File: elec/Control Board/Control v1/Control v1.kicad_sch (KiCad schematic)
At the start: 24 parts, among them J10 Conn_02x12_Odd_Even, J12 Screw_Terminal_01x02, J13 Screw_Terminal_01x02, J14 Screw_Terminal_01x02, J2 DB9_Female_MountingHoles, J3 Conn_01x08, J4 Conn_01x08, J5 Conn_01x08, J6 Conn_01x08, J7 Conn_01x08, J8 Conn_02x18_Odd_Even, J9 Conn_01x10_MountingPin

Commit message: Add footrpint to Max31850 module.
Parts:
- renumbered J2 to J1, J12 to J10, J13 to J11, J14 to J12, J3 to J2, J4 to J3, J5 to J4, J6 to J5, J7 to J6, J8 to J7, J9 to J8, J10 to J9
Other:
- note removed: "A change."
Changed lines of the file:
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@@
     (effects (font (size 0.635 0.635)) (justify left bottom))
-  )
-  (text "A change." (at 365.76 125.73 0)
-    (effects (font (size 1.27 1.27)) (justify left bottom))
   )
   (text "To chassis mounted +24V." (at 403.86 224.79 0)
@@
     )
   )
-  (global_label "aGlobal" (shape input) (at 325.12 69.85 0) (fields_autoplaced)
-    (effects (font (size 1.27 1.27)) (justify left))
-    (property "Intersheetrefs" "${INTERSHEET_REFS}" (at 335.2222 69.85 0)
-      (effects (font (size 1.27 1.27)) (justify left) hide)
-    )
-  )
   (global_label "BLOWER_TACH" (shape input) (at 316.23 199.39 180) (fields_autoplaced)
     (effects (font (size 1.27 1.27)) (justify right))
@@
   (symbol (lib_id "Connector_Generic:Conn_02x18_Odd_Even") (at 275.59 138.43 0) (unit 1)
     (in_bom yes) (on_board yes) (dnp no) (fields_autoplaced)
-    (property "Reference" "J8" (at 276.86 111.76 0)
+    (property "Reference" "J7" (at 276.86 111.76 0)
       (effects (font (size 1.27 1.27)))
     )
@@
       (project "Control v1"
         (path "/c68c9deb-8d4d-42f0-adf8-4d3022f4ee59"
-          (reference "J8") (unit 1)
+          (reference "J7") (unit 1)
         )
       )
@@
   (symbol (lib_id "Connector:Screw_Terminal_01x02") (at 394.97 226.06 0) (unit 1)
     (in_bom yes) (on_board yes) (dnp no) (fields_autoplaced)
-    (property "Reference" "J13" (at 397.51 226.695 0)
+    (property "Reference" "J11" (at 397.51 226.695 0)
       (effects (font (size 1.27 1.27)) (justify left))
     )
@@
       (project "Control v1"
         (path "/c68c9deb-8d4d-42f0-adf8-4d3022f4ee59"
-          (reference "J13") (unit 1)
+          (reference "J11") (unit 1)
         )
       )
@@
   (symbol (lib_id "power:+12V") (at 382.27 190.5 0) (unit 1)
     (in_bom yes) (on_board yes) (dnp no) (fields_autoplaced)
-    (property "Reference" "#PWR017" (at 382.27 194.31 0)
+    (property "Reference" "#PWR016" (at 382.27 194.31 0)
       (effects (font (size 1.27 1.27)) hide)
     )
@@
       (project "Control v1"
         (path "/c68c9deb-8d4d-42f0-adf8-4d3022f4ee59"
-          (reference "#PWR017") (unit 1)
+          (reference "#PWR016") (unit 1)
         )
       )
@@
   (symbol (lib_id "Connector_Generic:Conn_01x08") (at 147.32 133.35 0) (mirror y) (unit 1)
     (in_bom yes) (on_board yes) (dnp no) (fields_autoplaced)
-    (property "Reference" "J4" (at 147.32 119.38 0)
+    (property "Reference" "J3" (at 147.32 119.38 0)
       (effects (font (size 1.27 1.27)))
     )
@@
       (project "Control v1"
         (path "/c68c9deb-8d4d-42f0-adf8-4d3022f4ee59"
-          (reference "J4") (unit 1)
+          (reference "J3") (unit 1)
         )
       )
@@
   (symbol (lib_id "Connector_Generic:Conn_01x08") (at 139.7 72.39 180) (unit 1)
     (in_bom yes) (on_board yes) (dnp no) (fields_autoplaced)
-    (property "Reference" "J3" (at 139.7 55.88 0)
+    (property "Reference" "J2" (at 139.7 55.88 0)
       (effects (font (size 1.27 1.27)))
     )
@@
       (project "Control v1"
         (path "/c68c9deb-8d4d-42f0-adf8-4d3022f4ee59"
-          (reference "J3") (unit 1)
+          (reference "J2") (unit 1)
         )
       )
@@
   (symbol (lib_id "power:GND") (at 382.27 231.14 0) (unit 1)
     (in_bom yes) (on_board yes) (dnp no) (fields_autoplaced)
-    (property "Reference" "#PWR020" (at 382.27 237.49 0)
+    (property "Reference" "#PWR019" (at 382.27 237.49 0)
       (effects (font (size 1.27 1.27)) hide)
     )
@@
       (project "Control v1"
         (path "/c68c9deb-8d4d-42f0-adf8-4d3022f4ee59"
-          (reference "#PWR020") (unit 1)
+          (reference "#PWR019") (unit 1)
         )
       )
@@
         )
         (path "/c68c9deb-8d4d-42f0-adf8-4d3022f4ee59"
-          (reference "R51") (unit 1)
+          (reference "R4") (unit 1)
         )
       )
@@
   (symbol (lib_id "power:+24V") (at 328.93 228.6 0) (unit 1)
     (in_bom yes) (on_board yes) (dnp no) (fields_autoplaced)
-    (property "Reference" "#PWR037" (at 328.93 232.41 0)
+    (property "Reference" "#PWR014" (at 328.93 232.41 0)
       (effects (font (size 1.27 1.27)) hide)
     )
@@
       (project "Control v1"
         (path "/c68c9deb-8d4d-42f0-adf8-4d3022f4ee59"
-          (reference "#PWR037") (unit 1)
+          (reference "#PWR014") (unit 1)
         )
       )
@@
   (symbol (lib_id "Connector_Generic:Conn_01x08") (at 154.94 113.03 0) (mirror y) (unit 1)
     (in_bom yes) (on_board yes) (dnp no)
-    (property "Reference" "J6" (at 149.86 109.22 0)
+    (property "Reference" "J5" (at 149.86 109.22 0)
       (effects (font (size 1.27 1.27)))
     )
@@
       (project "Control v1"
         (path "/c68c9deb-8d4d-42f0-adf8-4d3022f4ee59"
-          (reference "J6") (unit 1)
+          (reference "J5") (unit 1)
         )
       )
@@
   (symbol (lib_id "Connector_Generic:Conn_01x08") (at 147.32 161.29 0) (mirror y) (unit 1)
     (in_bom yes) (on_board yes) (dnp no)
-    (property "Reference" "J5" (at 142.24 161.29 0)
+    (property "Reference" "J4" (at 142.24 161.29 0)
       (effects (font (size 1.27 1.27)))
     )
@@
       (project "Control v1"
         (path "/c68c9deb-8d4d-42f0-adf8-4d3022f4ee59"
-          (reference "J5") (unit 1)
+          (reference "J4") (unit 1)
         )
       )
@@
   (symbol (lib_id "Connector_Generic_MountingPin:Conn_01x10_MountingPin") (at 284.48 90.17 0) (mirror x) (unit 1)
     (in_bom yes) (on_board yes) (dnp no)
-    (property "Reference" "J9" (at 276.86 67.31 0)
+    (property "Reference" "J8" (at 276.86 67.31 0)
       (effects (font (size 1.27 1.27)) (justify left))
     )
@@
       (project "Control v1"
         (path "/c68c9deb-8d4d-42f0-adf8-4d3022f4ee59"
-          (reference "J9") (unit 1)
+          (reference "J8") (unit 1)
         )
       )
@@
   (symbol (lib_id "Connector:Screw_Terminal_01x02") (at 394.97 194.31 0) (unit 1)
     (in_bom yes) (on_board yes) (dnp no) (fields_autoplaced)
-    (property "Reference" "J12" (at 397.51 194.945 0)
+    (property "Reference" "J10" (at 397.51 194.945 0)
       (effects (font (size 1.27 1.27)) (justify left))
     )
@@
       (project "Control v1"
         (path "/c68c9deb-8d4d-42f0-adf8-4d3022f4ee59"
-          (reference "J12") (unit 1)
+          (reference "J10") (unit 1)
         )
       )
@@
   (symbol (lib_id "Connector_Generic:Conn_02x12_Odd_Even") (at 367.03 78.74 0) (mirror y) (unit 1)
     (in_bom yes) (on_board yes) (dnp no)
-    (property "Reference" "J10" (at 365.76 60.96 0)
+    (property "Reference" "J9" (at 365.76 60.96 0)
       (effects (font (size 1.27 1.27)))
     )
@@
       (project "Control v1"
         (path "/c68c9deb-8d4d-42f0-adf8-4d3022f4ee59"
-          (reference "J10") (unit 1)
+          (reference "J9") (unit 1)
         )
       )
@@
   (symbol (lib_id "power:GND") (at 382.27 203.2 0) (unit 1)
     (in_bom yes) (on_board yes) (dnp no) (fields_autoplaced)
-    (property "Reference" "#PWR018" (at 382.27 209.55 0)
+    (property "Reference" "#PWR017" (at 382.27 209.55 0)
       (effects (font (size 1.27 1.27)) hide)
     )
@@
       (project "Control v1"
         (path "/c68c9deb-8d4d-42f0-adf8-4d3022f4ee59"
-          (reference "#PWR018") (unit 1)
+          (reference "#PWR017") (unit 1)
         )
       )
@@
   (symbol (lib_id "Connector:Screw_Terminal_01x02") (at 394.97 237.49 0) (unit 1)
     (in_bom yes) (on_board yes) (dnp no) (fields_autoplaced)
-    (property "Reference" "J14" (at 397.51 238.125 0)
+    (property "Reference" "J12" (at 397.51 238.125 0)
       (effects (font (size 1.27 1.27)) (justify left))
     )
@@
       (project "Control v1"
         (path "/c68c9deb-8d4d-42f0-adf8-4d3022f4ee59"
-          (reference "J14") (unit 1)
+          (reference "J12") (unit 1)
         )
       )
@@
   (symbol (lib_id "Connector:DB9_Female_MountingHoles") (at 59.69 71.12 180) (unit 1)
     (in_bom yes) (on_board yes) (dnp no) (fields_autoplaced)
-    (property "Reference" "J2" (at 54.61 69.8499 0)
+    (property "Reference" "J1" (at 54.61 69.8499 0)
       (effects (font (size 1.27 1.27)) (justify left))
     )
@@
       (project "Control v1"
         (path "/c68c9deb-8d4d-42f0-adf8-4d3022f4ee59"
-          (reference "J2") (unit 1)
+          (reference "J1") (unit 1)
         )
       )
@@
         )
         (path "/c68c9deb-8d4d-42f0-adf8-4d3022f4ee59"
-          (reference "R52") (unit 1)
+          (reference "R5") (unit 1)
         )
       )
@@
   (symbol (lib_id "power:+24V") (at 382.27 223.52 0) (unit 1)
     (in_bom yes) (on_board yes) (dnp no) (fields_autoplaced)
-    (property "Reference" "#PWR019" (at 382.27 227.33 0)
+    (property "Reference" "#PWR018" (at 382.27 227.33 0)
       (effects (font (size 1.27 1.27)) hide)
     )
@@
       (project "Control v1"
         (path "/c68c9deb-8d4d-42f0-adf8-4d3022f4ee59"
-          (reference "#PWR019") (unit 1)
+          (reference "#PWR018") (unit 1)
         )
       )
@@
   (symbol (lib_id "Connector_Generic:Conn_01x08") (at 269.24 64.77 0) (unit 1)
     (in_bom yes) (on_board yes) (dnp no)
-    (property "Reference" "J7" (at 259.08 50.8 0)
+    (property "Reference" "J6" (at 259.08 50.8 0)
       (effects (font (size 1.27 1.27)) (justify left))
     )
@@
       (project "Control v1"
         (path "/c68c9deb-8d4d-42f0-adf8-4d3022f4ee59"
-          (reference "J7") (unit 1)
-        )
-      )
+          (reference "J6") (unit 1)
+        )
+      )

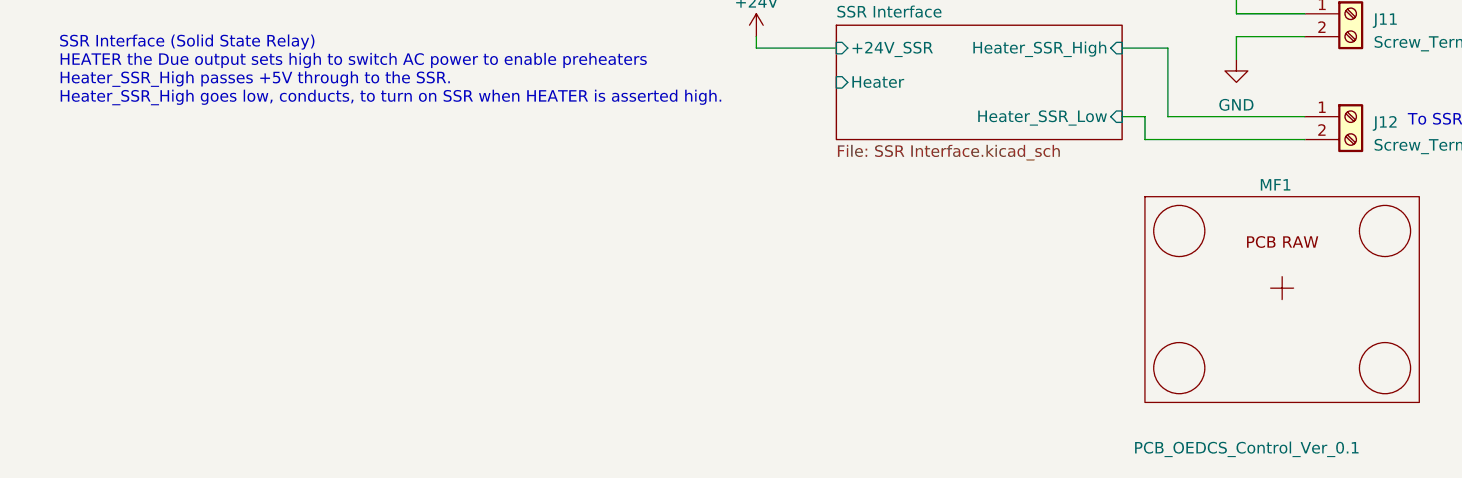
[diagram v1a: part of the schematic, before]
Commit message: Add footprints for thermoucouple modules to schematic and PCB.  This commit does NOT capture the library changes.
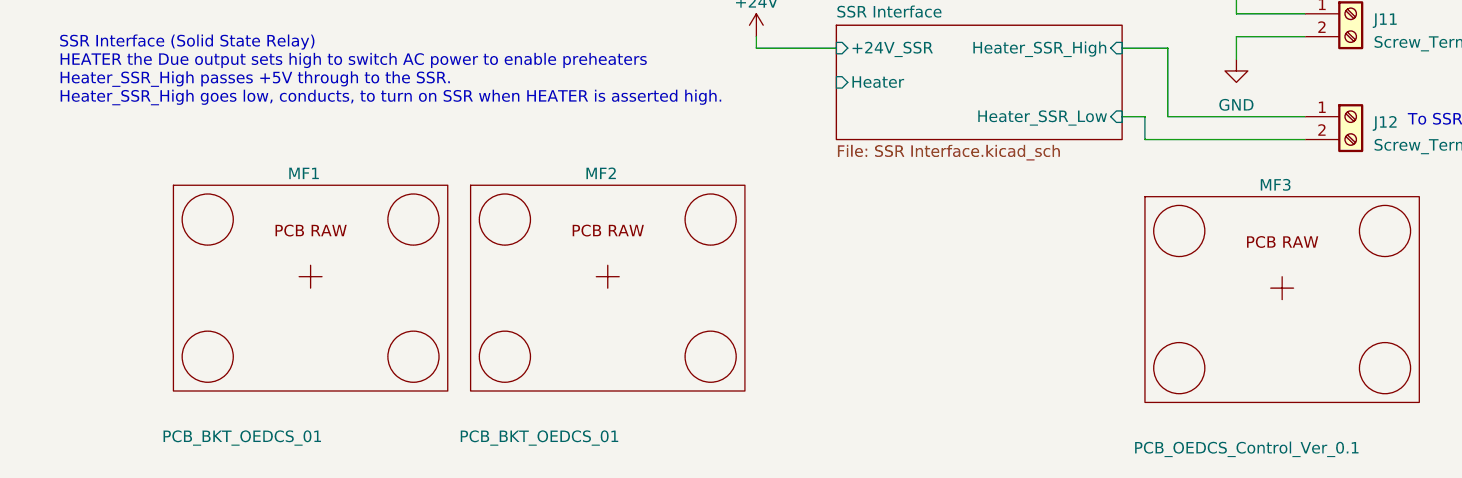
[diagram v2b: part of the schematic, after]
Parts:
- added MF1, MF2: PCB_BKT_OEDCS_01, NA, symbol GPAD_SCH_LIB:PCB_GPAD_VER1
- renumbered MF1 to MF3
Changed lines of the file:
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@@
   (symbol (lib_id "GPAD_SCH_LIB:PCB_GPAD_VER1") (at 387.35 256.54 0) (unit 1)
     (in_bom yes) (on_board no) (dnp no)
-    (property "Reference" "MF1" (at 384.81 245.11 0)
+    (property "Reference" "MF3" (at 384.81 245.11 0)
       (effects (font (size 1.27 1.27)) (justify left))
     )
@@
       (project "Control v1"
         (path "/c68c9deb-8d4d-42f0-adf8-4d3022f4ee59"
-          (reference "MF1") (unit 1)
+          (reference "MF3") (unit 1)
         )
       )
@@
     )
   )
+  (symbol (lib_id "GPAD_SCH_LIB:PCB_GPAD_VER1") (at 279.4 255.27 0) (unit 1)
+    (in_bom yes) (on_board no) (dnp no)
+    (property "Reference" "MF1" (at 276.86 243.84 0)
+      (effects (font (size 1.27 1.27)) (justify left))
+    )
+    (property "Value" "PCB_BKT_OEDCS_01" (at 262.89 273.05 0)
+      (effects (font (size 1.27 1.27)) (justify left))
+    )
+    (property "Footprint" "NA" (at 279.4 255.27 0)
+      (effects (font (size 1.27 1.27)) hide)
+    )
+    (property "Datasheet" "PCB_BKT_OEDCS_01" (at 279.4 255.27 0)
+      (effects (font (size 0 0)) hide)
+    )
+    (property "Distributor 1" "PublicInvention" (at 279.4 255.27 0)
+      (effects (font (size 1.27 1.27)) hide)
+    )
+    (property "Distributor 1 PN" "PCB_BKT_OEDCS_01" (at 279.4 255.27 0)
+      (effects (font (size 0 0)) hide)
+    )
+    (property "Cost" "1000000" (at 279.4 255.27 0)
+      (effects (font (size 1.27 1.27)) hide)
+    )
+    (property "AssemblyType" "HAND" (at 279.4 255.27 0)
+      (effects (font (size 1.27 1.27)) hide)
+    )
+    (property "Description" "PCB_BKT_OEDCS_01" (at 279.4 255.27 0)
+      (effects (font (size 1.27 1.27)) hide)
+    )
+    (property "MPN" "PCB_BKT_OEDCS_01" (at 279.4 255.27 0)
+      (effects (font (size 1.27 1.27)) hide)
+    )
+    (property "LongLead" "YES" (at 279.4 255.27 0)
+      (effects (font (size 1.27 1.27)) hide)
+    )
+    (property "Manufacturer" "PublicInvention" (at 279.4 255.27 0)
+      (effects (font (size 1.27 1.27)) hide)
+    )
+    (instances
+      (project "Control v1"
+        (path "/c68c9deb-8d4d-42f0-adf8-4d3022f4ee59"
+          (reference "MF1") (unit 1)
+        )
+      )
+    )
+  )
   (symbol (lib_id "Device:R") (at 342.9 87.63 90) (mirror x) (unit 1)
     (in_bom yes) (on_board yes) (dnp no)
@@
         )
       )
+    )
+  )
+  (symbol (lib_id "GPAD_SCH_LIB:PCB_GPAD_VER1") (at 312.42 255.27 0) (unit 1)
+    (in_bom yes) (on_board no) (dnp no)
+    (property "Reference" "MF2" (at 309.88 243.84 0)
+      (effects (font (size 1.27 1.27)) (justify left))
+    )
+    (property "Value" "PCB_BKT_OEDCS_01" (at 295.91 273.05 0)
+      (effects (font (size 1.27 1.27)) (justify left))
+    )
+    (property "Footprint" "NA" (at 312.42 255.27 0)
+      (effects (font (size 1.27 1.27)) hide)
+    )
+    (property "Datasheet" "PCB_BKT_OEDCS_01" (at 312.42 255.27 0)
+      (effects (font (size 0 0)) hide)
+    )
+    (property "Distributor 1" "PublicInvention" (at 312.42 255.27 0)
+      (effects (font (size 1.27 1.27)) hide)
+    )
+    (property "Distributor 1 PN" "PCB_BKT_OEDCS_01" (at 312.42 255.27 0)
+      (effects (font (size 0 0)) hide)
+    )
+    (property "Cost" "1000000" (at 312.42 255.27 0)
+      (effects (font (size 1.27 1.27)) hide)
+    )
+    (property "AssemblyType" "HAND" (at 312.42 255.27 0)
+      (effects (font (size 1.27 1.27)) hide)
+    )
+    (property "Description" "PCB_BKT_OEDCS_01" (at 312.42 255.27 0)
+      (effects (font (size 1.27 1.27)) hide)
+    )
+    (property "MPN" "PCB_BKT_OEDCS_01" (at 312.42 255.27 0)
+      (effects (font (size 1.27 1.27)) hide)
+    )
+    (property "LongLead" "YES" (at 312.42 255.27 0)
+      (effects (font (size 1.27 1.27)) hide)
+    )
+    (property "Manufacturer" "PublicInvention" (at 312.42 255.27 0)
+      (effects (font (size 1.27 1.27)) hide)
+    )
+    (instances
+      (project "Control v1"
+        (path "/c68c9deb-8d4d-42f0-adf8-4d3022f4ee59"
+          (reference "MF2") (unit 1)
+        )
+      )
